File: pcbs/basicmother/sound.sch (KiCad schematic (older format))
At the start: 19 parts

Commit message: Actualizo esquematico de la placa principal y empiezo con el layout
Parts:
- removed C?: 10 uF, symbol CAPAPOL
- removed C?: 47n, symbol C
- removed C? (x3): 100 nF, symbol C
- removed C? (x2): 18n, symbol C
- removed C?: 3.3 uF, symbol CAPAPOL
- removed L? (x2): 1 uH, symbol INDUCTOR_SMALL
- removed P?: speaker, symbol CONN_01X02
- removed R? (x2): 2.2k, symbol R
- removed R?: 10, symbol R
- removed RV?: 10k, symbol POT
- removed U?: LM386, symbol LM386
- removed U? (x2): TL082, symbol TL082
- added C12, C13: 390n, Capacitors_ThroughHole:C_Disc_D3_P2.5, symbol C
- added C14, C15: 10u, Capacitors_ThroughHole:C_Radial_D5_L6_P2.5, symbol CAPAPOL
- added C16, C17: 1u, Capacitors_ThroughHole:C_Disc_D3_P2.5, symbol C
- added L2: 1 uH, Resistors_ThroughHole:Resistor_Horizontal_RM10mm, symbol INDUCTOR_SMALL
- added P8, P9: CONN_01X02, Pin_Headers:Pin_Header_Straight_1x02, symbol CONN_01X02
- added R10, R5, R6, R7, R8, R9: 22k, Resistors_ThroughHole:Resistor_Horizontal_RM10mm, symbol R
- added RV1, RV2: POT, Socket_Strips:Socket_Strip_Straight_1x03, symbol POT
- added U5, U6: LM4950TS, Popurri_CDR:TO-263, symbol LM4950TS
- L1: renamed from L?; footprint (none) -> Resistors_ThroughHole:Resistor_Horizontal_RM10mm
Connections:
- net labels added: IN, VIN, ~SHD
- net labels removed: 5V
- wire segments 80 -> 84
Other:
- moved on the sheet: L1

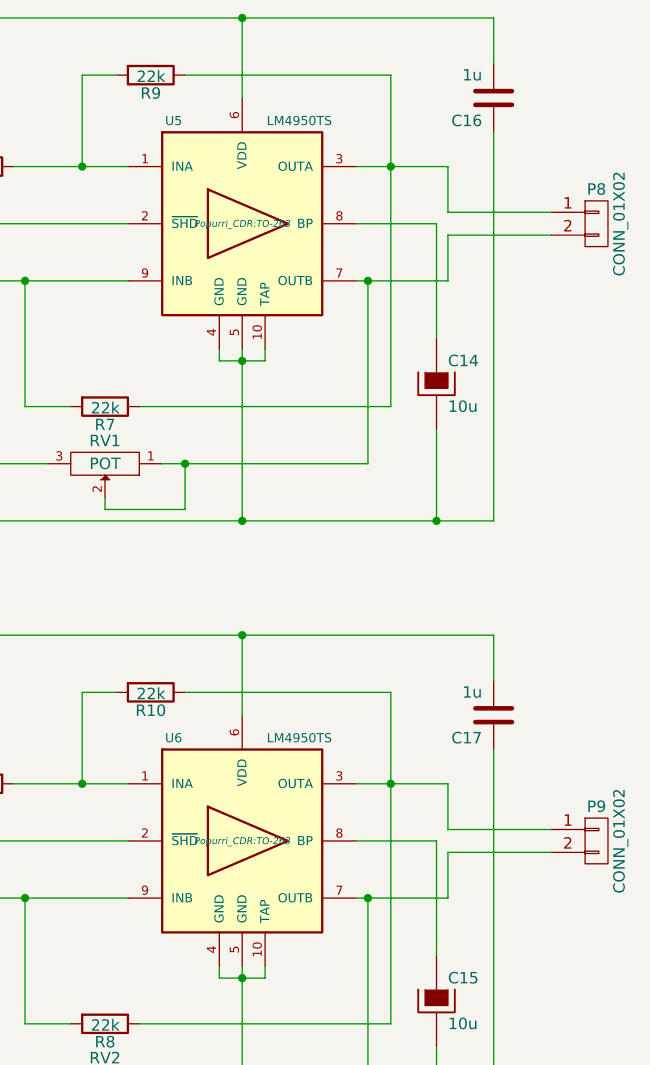
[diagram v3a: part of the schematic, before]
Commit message: Actualizo el esquematico de la placa principal
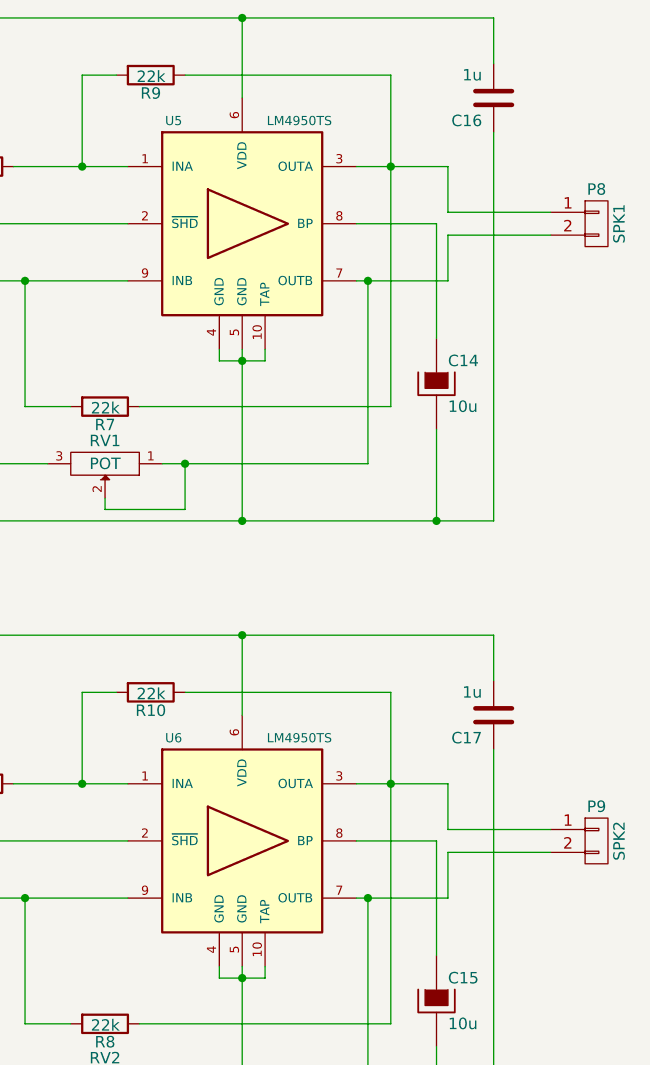
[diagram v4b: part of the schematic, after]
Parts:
- P8: value CONN_01X02 -> SPK1
- P9: value CONN_01X02 -> SPK2
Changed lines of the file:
@@
 F 0 "U5" H 5000 2600 40  0000 C CNN
 F 1 "LM4950TS" H 5550 2600 40  0000 C CNN
-F 2 "Popurri_CDR:TO-263" H 5300 2150 30  0000 C CIN
+F 2 "Popurri_CDR:TO-263" H 5300 2150 30  0001 C CIN
 F 3 "" H 5300 2150 60  0000 C CNN
 	1    5300 2150
@@
 P 6850 2150
 F 0 "P8" H 6850 2300 50  0000 C CNN
-F 1 "CONN_01X02" V 6950 2150 50  0000 C CNN
+F 1 "SPK1" V 6950 2150 50  0000 C CNN
 F 2 "Pin_Headers:Pin_Header_Straight_1x02" H 6850 2150 60  0001 C CNN
 F 3 "" H 6850 2150 60  0000 C CNN
@@
 F 0 "U6" H 5000 5300 40  0000 C CNN
 F 1 "LM4950TS" H 5550 5300 40  0000 C CNN
-F 2 "Popurri_CDR:TO-263" H 5300 4850 30  0000 C CIN
+F 2 "Popurri_CDR:TO-263" H 5300 4850 30  0001 C CIN
 F 3 "" H 5300 4850 60  0000 C CNN
 	1    5300 4850
@@
 P 6850 4850
 F 0 "P9" H 6850 5000 50  0000 C CNN
-F 1 "CONN_01X02" V 6950 4850 50  0000 C CNN
+F 1 "SPK2" V 6950 4850 50  0000 C CNN
 F 2 "Pin_Headers:Pin_Header_Straight_1x02" H 6850 4850 60  0001 C CNN
 F 3 "" H 6850 4850 60  0000 C CNN

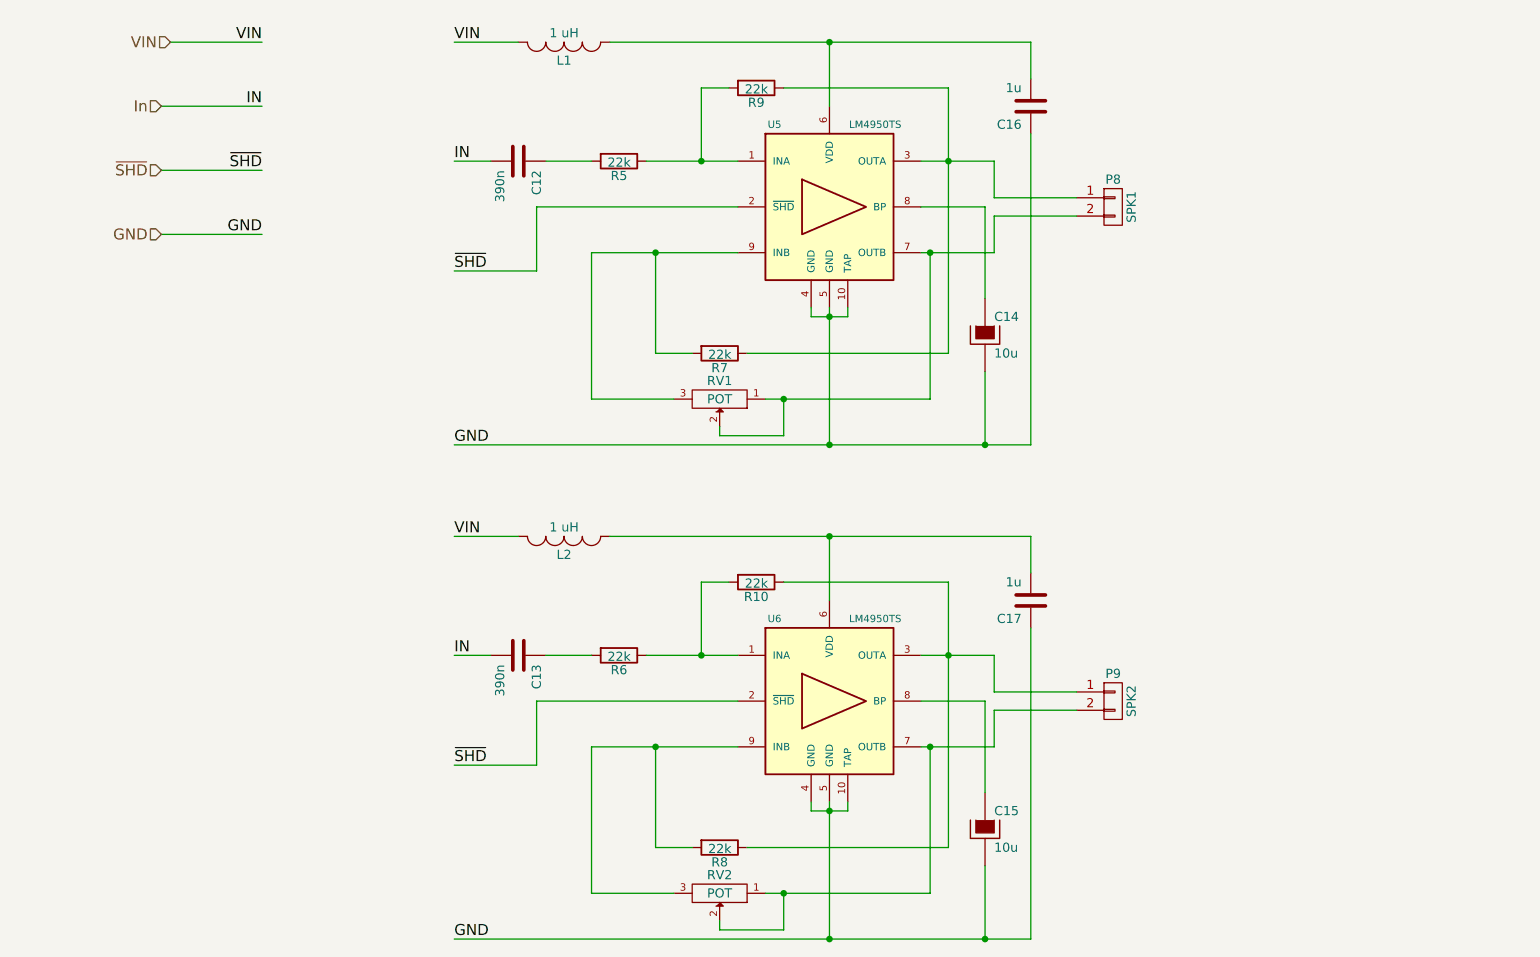
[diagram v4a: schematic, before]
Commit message: saque el micro para el control de los ojitos y lo pase a una placa aparte, ademas agregue un doble microfono
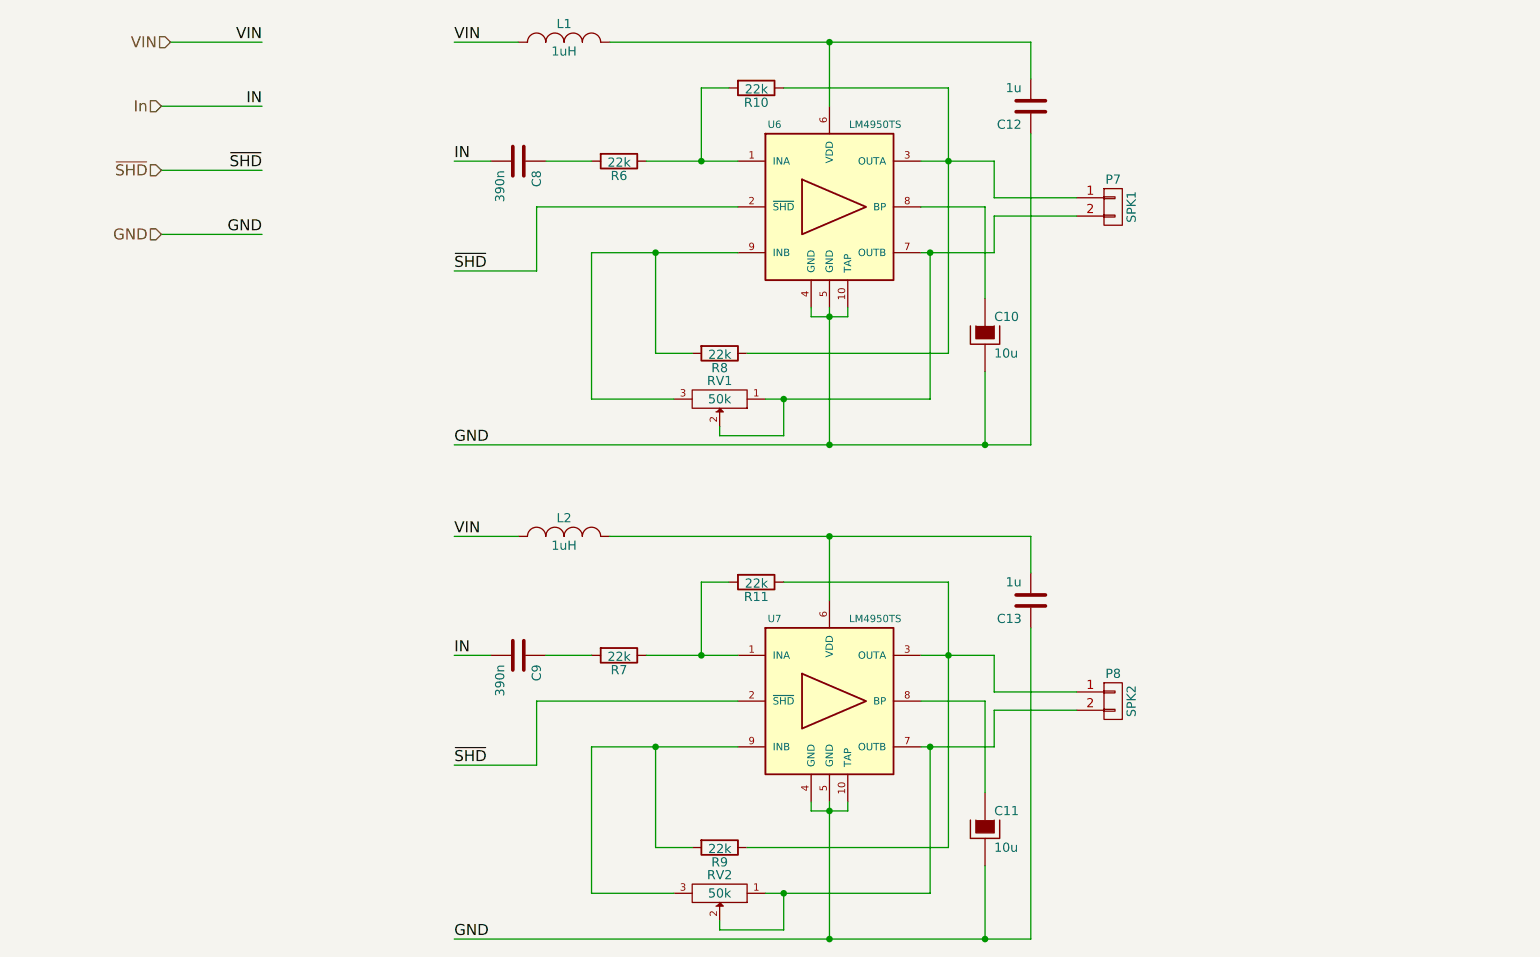
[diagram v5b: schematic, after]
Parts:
- L1, L2: value 1 uH -> 1uH
- P7: renamed from P8; footprint Pin_Headers:Pin_Header_Straight_1x02 -> Socket_Strips:Socket_Strip_Straight_1x02
- P8: renamed from P9; footprint Pin_Headers:Pin_Header_Straight_1x02 -> Socket_Strips:Socket_Strip_Straight_1x02
- RV1, RV2: value POT -> 50k
- renumbered C14 to C10, C15 to C11, C16 to C12, C17 to C13, C12 to C8, C13 to C9, R9 to R10, R10 to R11, R5 to R6, R6 to R7, R7 to R8, R8 to R9, U5 to U6, U6 to U7
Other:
- moved on the sheet: L1, L2
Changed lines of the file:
@@
 P 3850 1250
 F 0 "L1" H 3850 1350 50  0000 C CNN
-F 1 "1 uH" H 3850 1200 50  0000 C CNN
+F 1 "1uH" H 3850 1200 50  0000 C CNN
 F 2 "Resistors_ThroughHole:Resistor_Horizontal_RM10mm" H 3850 1250 60  0001 C CNN
 F 3 "" H 3850 1250 60  0000 C CNN
 	1    3850 1250
-	-1   0    0    1
+	-1   0    0    -1
 $EndComp
 Text HLabel 1650 1600 0    60   Input ~ 0
@@
 GND
 $Comp
-L LM4950TS U5
+L LM4950TS U6
 U 1 1 5503745D
 P 5300 2150
-F 0 "U5" H 5000 2600 40  0000 C CNN
+F 0 "U6" H 5000 2600 40  0000 C CNN
 F 1 "LM4950TS" H 5550 2600 40  0000 C CNN
 F 2 "Popurri_CDR:TO-263" H 5300 2150 30  0001 C CIN
@@
 $EndComp
 $Comp
-L R R9
+L R R10
 U 1 1 55037556
 P 4900 1500
-F 0 "R9" V 4980 1500 50  0000 C CNN
+F 0 "R10" V 4980 1500 50  0000 C CNN
 F 1 "22k" V 4907 1501 50  0000 C CNN
 F 2 "Resistors_ThroughHole:Resistor_Horizontal_RM10mm" V 4830 1500 30  0001 C CNN
@@
 Connection ~ 4600 1900
 $Comp
-L R R5
+L R R6
 U 1 1 550376F5
 P 4150 1900
-F 0 "R5" V 4230 1900 50  0000 C CNN
+F 0 "R6" V 4230 1900 50  0000 C CNN
 F 1 "22k" V 4157 1901 50  0000 C CNN
 F 2 "Resistors_ThroughHole:Resistor_Horizontal_RM10mm" V 4080 1900 30  0001 C CNN
@@
 $EndComp
 $Comp
-L C C12
+L C C8
 U 1 1 5503774B
 P 3600 1900
-F 0 "C12" H 3650 2000 50  0000 L CNN
+F 0 "C8" H 3650 2000 50  0000 L CNN
 F 1 "390n" H 3650 1800 50  0000 L CNN
 F 2 "Capacitors_ThroughHole:C_Disc_D3_P2.5" H 3638 1750 30  0001 C CNN
@@
 Connection ~ 5950 1900
 $Comp
-L R R7
+L R R8
 U 1 1 550379F5
 P 4700 2950
-F 0 "R7" V 4780 2950 50  0000 C CNN
+F 0 "R8" V 4780 2950 50  0000 C CNN
 F 1 "22k" V 4707 2951 50  0000 C CNN
 F 2 "Resistors_ThroughHole:Resistor_Horizontal_RM10mm" V 4630 2950 30  0001 C CNN
@@
 Connection ~ 5850 2400
 $Comp
-L CONN_01X02 P8
+L CONN_01X02 P7
 U 1 1 55037E97
 P 6850 2150
-F 0 "P8" H 6850 2300 50  0000 C CNN
+F 0 "P7" H 6850 2300 50  0000 C CNN
 F 1 "SPK1" V 6950 2150 50  0000 C CNN
-F 2 "Pin_Headers:Pin_Header_Straight_1x02" H 6850 2150 60  0001 C CNN
+F 2 "Socket_Strips:Socket_Strip_Straight_1x02" H 6850 2150 60  0001 C CNN
 F 3 "" H 6850 2150 60  0000 C CNN
 	1    6850 2150
@@
 	6150 2150 6150 2650
 $Comp
-L CAPAPOL C14
+L CAPAPOL C10
 U 1 1 550394AA
 P 6150 2850
-F 0 "C14" H 6200 2950 50  0000 L CNN
+F 0 "C10" H 6200 2950 50  0000 L CNN
 F 1 "10u" H 6200 2750 50  0000 L CNN
 F 2 "Capacitors_ThroughHole:C_Radial_D5_L6_P2.5" H 6250 2700 30  0001 C CNN
@@
 P 4700 3200
 F 0 "RV1" H 4700 3100 50  0000 C CNN
-F 1 "POT" H 4700 3200 50  0000 C CNN
+F 1 "50k" H 4700 3200 50  0000 C CNN
 F 2 "Socket_Strips:Socket_Strip_Straight_1x03" H 4700 3200 60  0001 C CNN
 F 3 "" H 4700 3200 60  0000 C CNN
@@
 	4100 1250 6400 1250
 $Comp
-L C C16
+L C C12
 U 1 1 5503AE04
 P 6400 1600
-F 0 "C16" H 6450 1700 50  0000 L CNN
+F 0 "C12" H 6450 1700 50  0000 L CNN
 F 1 "1u" H 6450 1500 50  0000 L CNN
 F 2 "Capacitors_ThroughHole:C_Disc_D3_P2.5" H 6438 1450 30  0001 C CNN
@@
 P 3850 3950
 F 0 "L2" H 3850 4050 50  0000 C CNN
-F 1 "1 uH" H 3850 3900 50  0000 C CNN
+F 1 "1uH" H 3850 3900 50  0000 C CNN
 F 2 "Resistors_ThroughHole:Resistor_Horizontal_RM10mm" H 3850 3950 60  0001 C CNN
 F 3 "" H 3850 3950 60  0000 C CNN
 	1    3850 3950
-	-1   0    0    1
-$EndComp
-$Comp
-L LM4950TS U6
+	-1   0    0    -1
+$EndComp
+$Comp
+L LM4950TS U7
 U 1 1 5503D026
 P 5300 4850
-F 0 "U6" H 5000 5300 40  0000 C CNN
+F 0 "U7" H 5000 5300 40  0000 C CNN
 F 1 "LM4950TS" H 5550 5300 40  0000 C CNN
 F 2 "Popurri_CDR:TO-263" H 5300 4850 30  0001 C CIN
@@
 $EndComp
 $Comp
-L R R10
+L R R11
 U 1 1 5503D02C
 P 4900 4200
-F 0 "R10" V 4980 4200 50  0000 C CNN
+F 0 "R11" V 4980 4200 50  0000 C CNN
 F 1 "22k" V 4907 4201 50  0000 C CNN
 F 2 "Resistors_ThroughHole:Resistor_Horizontal_RM10mm" V 4830 4200 30  0001 C CNN
@@
 Connection ~ 4600 4600
 $Comp
-L R R6
+L R R7
 U 1 1 5503D036
 P 4150 4600
-F 0 "R6" V 4230 4600 50  0000 C CNN
+F 0 "R7" V 4230 4600 50  0000 C CNN
 F 1 "22k" V 4157 4601 50  0000 C CNN
 F 2 "Resistors_ThroughHole:Resistor_Horizontal_RM10mm" V 4080 4600 30  0001 C CNN
@@
 $EndComp
 $Comp
-L C C13
+L C C9
 U 1 1 5503D03C
 P 3600 4600
-F 0 "C13" H 3650 4700 50  0000 L CNN
+F 0 "C9" H 3650 4700 50  0000 L CNN
 F 1 "390n" H 3650 4500 50  0000 L CNN
 F 2 "Capacitors_ThroughHole:C_Disc_D3_P2.5" H 3638 4450 30  0001 C CNN
@@
 Connection ~ 5950 4600
 $Comp
-L R R8
+L R R9
 U 1 1 5503D049
 P 4700 5650
-F 0 "R8" V 4780 5650 50  0000 C CNN
+F 0 "R9" V 4780 5650 50  0000 C CNN
 F 1 "22k" V 4707 5651 50  0000 C CNN
 F 2 "Resistors_ThroughHole:Resistor_Horizontal_RM10mm" V 4630 5650 30  0001 C CNN
@@
 Connection ~ 5850 5100
 $Comp
-L CONN_01X02 P9
+L CONN_01X02 P8
 U 1 1 5503D05B
 P 6850 4850
-F 0 "P9" H 6850 5000 50  0000 C CNN
+F 0 "P8" H 6850 5000 50  0000 C CNN
 F 1 "SPK2" V 6950 4850 50  0000 C CNN
-F 2 "Pin_Headers:Pin_Header_Straight_1x02" H 6850 4850 60  0001 C CNN
+F 2 "Socket_Strips:Socket_Strip_Straight_1x02" H 6850 4850 60  0001 C CNN
 F 3 "" H 6850 4850 60  0000 C CNN
 	1    6850 4850
@@
 	6150 4850 6150 5350
 $Comp
-L CAPAPOL C15
+L CAPAPOL C11
 U 1 1 5503D065
 P 6150 5550
-F 0 "C15" H 6200 5650 50  0000 L CNN
+F 0 "C11" H 6200 5650 50  0000 L CNN
 F 1 "10u" H 6200 5450 50  0000 L CNN
 F 2 "Capacitors_ThroughHole:C_Radial_D5_L6_P2.5" H 6250 5400 30  0001 C CNN
@@
 P 4700 5900
 F 0 "RV2" H 4700 5800 50  0000 C CNN
-F 1 "POT" H 4700 5900 50  0000 C CNN
+F 1 "50k" H 4700 5900 50  0000 C CNN
 F 2 "Socket_Strips:Socket_Strip_Straight_1x03" H 4700 5900 60  0001 C CNN
 F 3 "" H 4700 5900 60  0000 C CNN
@@
 	4100 3950 6400 3950
 $Comp
-L C C17
+L C C13
 U 1 1 5503D082
 P 6400 4300
-F 0 "C17" H 6450 4400 50  0000 L CNN
+F 0 "C13" H 6450 4400 50  0000 L CNN
 F 1 "1u" H 6450 4200 50  0000 L CNN
 F 2 "Capacitors_ThroughHole:C_Disc_D3_P2.5" H 6438 4150 30  0001 C CNN

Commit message: actualizo las 3 placas, revisar y mandar a fabricar
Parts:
- C12, C13: footprint Capacitors_ThroughHole:C_Disc_D3_P2.5 -> Capacitors_ThroughHole:C_Rect_L18_W5_P15
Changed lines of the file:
@@
 F 0 "C12" H 6450 1700 50  0000 L CNN
 F 1 "1u" H 6450 1500 50  0000 L CNN
-F 2 "Capacitors_ThroughHole:C_Disc_D3_P2.5" H 6438 1450 30  0001 C CNN
+F 2 "Capacitors_ThroughHole:C_Rect_L18_W5_P15" H 6438 1450 30  0001 C CNN
 F 3 "" H 6400 1600 60  0000 C CNN
 	1    6400 1600
@@
 F 0 "C13" H 6450 4400 50  0000 L CNN
 F 1 "1u" H 6450 4200 50  0000 L CNN
-F 2 "Capacitors_ThroughHole:C_Disc_D3_P2.5" H 6438 4150 30  0001 C CNN
+F 2 "Capacitors_ThroughHole:C_Rect_L18_W5_P15" H 6438 4150 30  0001 C CNN
 F 3 "" H 6400 4300 60  0000 C CNN
 	1    6400 4300
